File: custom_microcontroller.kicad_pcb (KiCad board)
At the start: 2 copper layers, 27.9 x 50.8 mm, 29 parts, among them J1 Conn_01x05_Male, J2 Conn_01x02_Male, J3 Conn_01x08_Male, J4 Conn_01x02_Male, J5 Conn_01x02_Male, J6 Conn_01x06_Male, J7 Conn_01x02_Male, U1 NCP1117ST33T3G, U2 STM32F042G6Ux, U3 SN65HVD233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

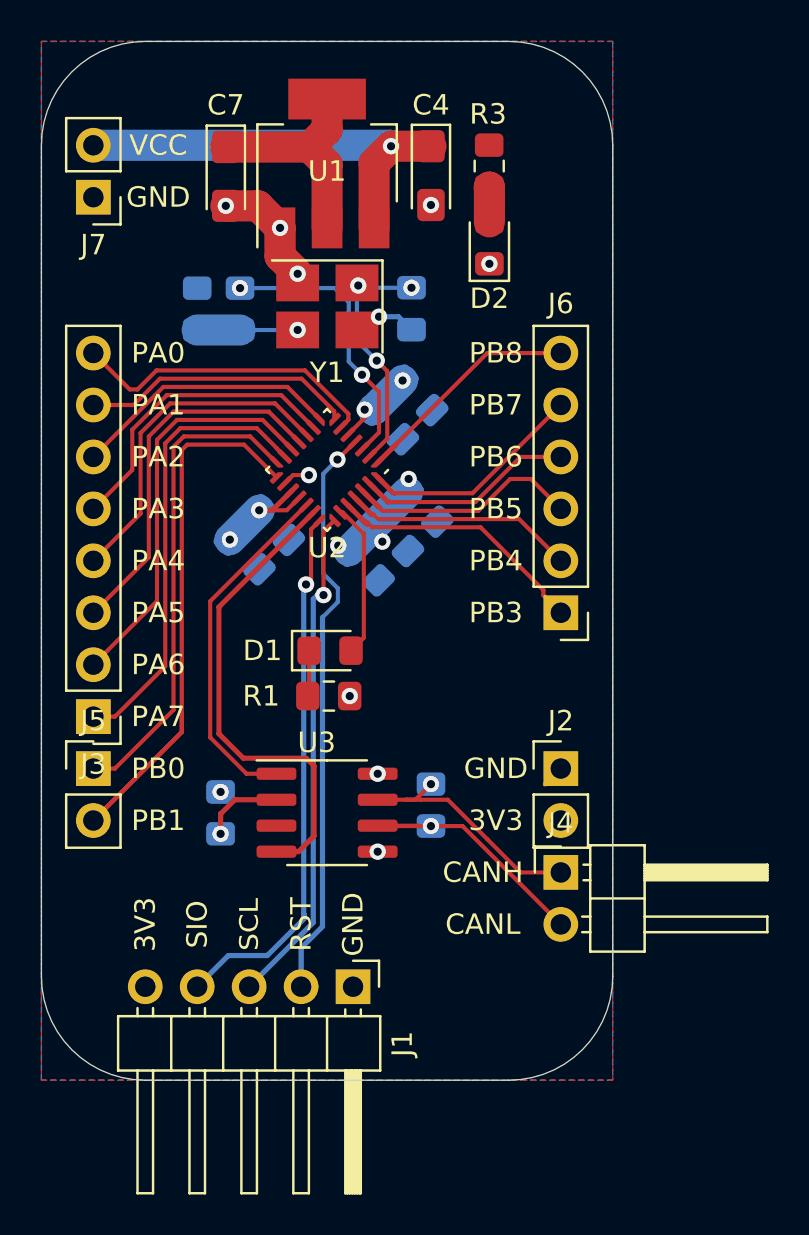
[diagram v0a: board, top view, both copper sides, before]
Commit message: panelized board
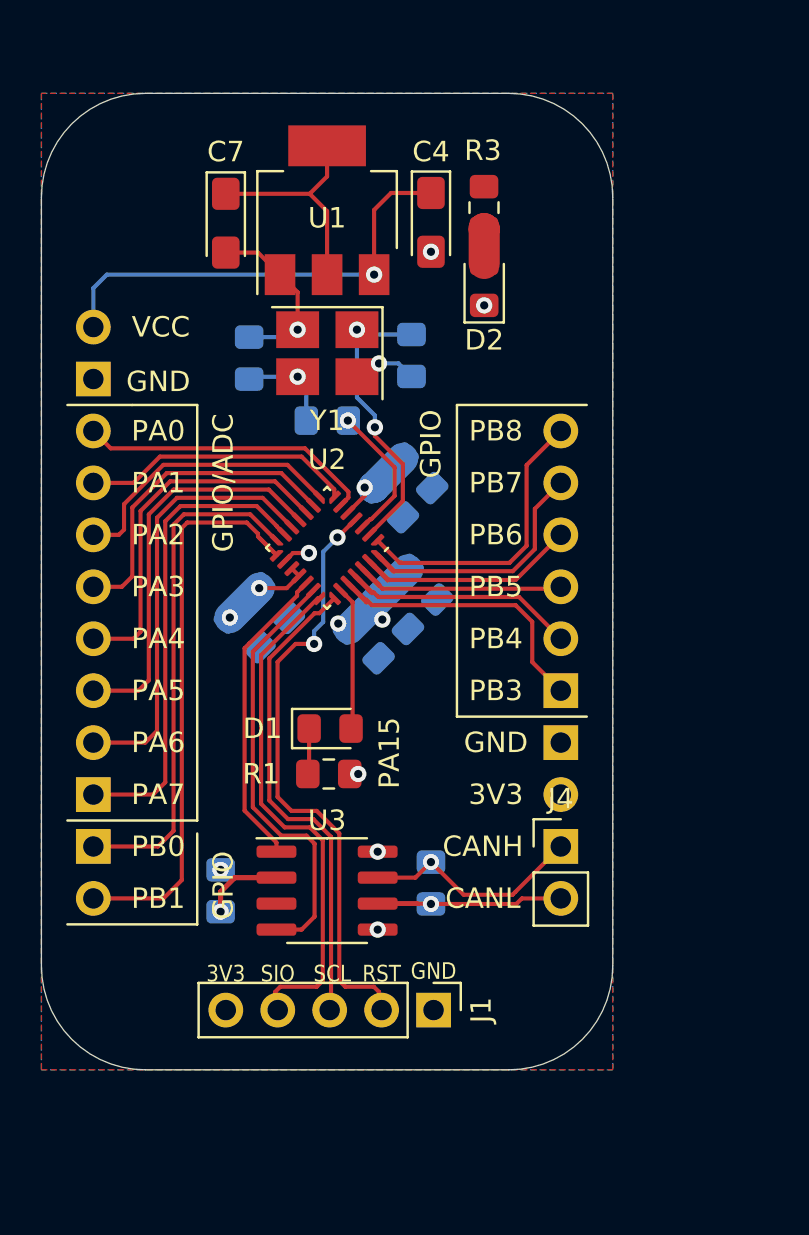
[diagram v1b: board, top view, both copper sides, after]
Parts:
- J1: footprint Connector_PinHeader_2.54mm:PinHeader_1x05_P2.54mm_Horizontal -> Connector_PinHeader_2.54mm:PinHeader_1x05_P2.54mm_Vertical
- J2, J3, J5, J6, J7: moved to B.Cu
- J4: footprint Connector_PinHeader_2.54mm:PinHeader_1x02_P2.54mm_Horizontal -> Connector_PinHeader_2.54mm:PinHeader_1x02_P2.54mm_Vertical
- moved J7 8.89 mm to (127.0, 120.7), turned to 0 degrees
- moved R2 6.92 mm to (138.4, 122.7), turned to 180 degrees
- moved J1 4.10 mm to (143.6, 151.5)
- moved C1 3.81 mm to (134.4, 133.0)
- moved C11 3.81 mm to (141.7, 132.1)
- moved C12 3.81 mm to (133.2, 145.7)
- moved C8 3.81 mm to (141.4, 126.7)
- moved C9 3.81 mm to (140.2, 133.6)
- moved J3 3.81 mm to (127.0, 141.0), turned to 0 degrees
- moved J5 3.81 mm to (127.0, 143.5), turned to 180 degrees
- moved R4 3.81 mm to (143.5, 145.3)
- moved U2 3.81 mm to (138.4, 128.9)
- moved U3 3.81 mm to (138.4, 145.7)
- moved C10 3.81 mm to (143.1, 130.7)
- moved C5 3.81 mm to (135.8, 131.6)
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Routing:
- net /OSC_N: track 13.7 -> 6.86 mm, vias 2 -> 1
- net /PB1: track 32.3 -> 28.6 mm
- net +3V3: track 28.1 -> 25.6 mm, vias 8 -> 6
- net /OSC_P: track 12.0 -> 14.4 mm, vias 3 -> 2
- net /CAN_RX: track 23.6 -> 21.3 mm
- net /CAN_TX: track 17.3 -> 15.0 mm
- net /PB8: track 12.4 -> 14.4 mm
- net /CAN_N: track 12.9 -> 11.1 mm
- net /PA2: track 13.2 -> 14.6 mm
- net /PA6: track 19.9 -> 21.4 mm
- net GND: track 16.1 -> 17.6 mm, vias 11 -> 9
- net VCC: track 20.9 -> 22.2 mm
- net /NRST: track 28.5 -> 29.8 mm, vias 1 -> 2
- net /PA5: track 18.2 -> 19.5 mm
- net /PB0: track 23.8 -> 25.0 mm
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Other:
- board size 27.9 x 50.8 mm -> 27.9 x 47.8 mm
- board text added: "GPIO"
- board text added: "GPIO/ADC"
- board text added: "PA15"

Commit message: single layer design
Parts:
- added G***: LOGO, memes:little_creatures, B.Cu at (138.6, 116.6)
- C1, C10, C11, C12, C2, C3, C5, C6, C8, C9, R2, R4: moved to F.Cu
- moved C6 6.67 mm to (136.2, 125.6), turned to 180 degrees
- moved C1 5.54 mm to (136.0, 138.4), turned to 180 degrees
- moved C8 5.30 mm to (136.2, 127.6), turned to 180 degrees
- moved C12 5.20 mm to (136.0, 141.3), turned to 180 degrees
- moved R1 4.94 mm to (143.4, 139.0), turned to 270 degrees
- moved C5 4.72 mm to (136.0, 136.3), turned to 180 degrees
- moved U2 3.93 mm to (137.4, 132.7), turned to 270 degrees
- moved D1 2.84 mm to (141.1, 139.0), turned to 90 degrees
- moved C9 2.63 mm to (142.6, 134.8), turned to 0 degrees
- moved C11 1.08 mm to (142.6, 132.7), turned to 0 degrees
- moved R4 0.67 mm to (143.2, 145.9)
- moved C10 0.52 mm to (142.6, 130.7), turned to 0 degrees
- moved C2 0.34 mm to (142.2, 119.4)
- moved C3 0.25 mm to (134.6, 119.4)
- moved R2 0.21 mm to (138.5, 122.9)
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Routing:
- net GND: track 17.6 -> 1.26 mm, vias 9 -> 21
- net /PB1: track 28.6 -> 18.7 mm
- net /PA5: track 19.5 -> 9.75 mm
- net /PA6: track 21.4 -> 12.3 mm
- net /PA4: track 17.7 -> 8.91 mm
- net /PA7: track 23.3 -> 14.6 mm
- net /SWDIO: track 25.6 -> 18.1 mm
- net /PA3: track 15.7 -> 8.79 mm
- net /PB5: track 10.2 -> 16.8 mm
- net /CAN_RX: track 21.3 -> 15.2 mm
- net /SWCLK: track 23.8 -> 17.9 mm
- net /NRST: track 29.8 -> 25.5 mm
- net /PA2: track 14.6 -> 10.3 mm
- net /PB6: track 10.7 -> 14.7 mm
- net /CAN_TX: track 15.0 -> 11.0 mm
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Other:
- board text added: "An STM32F042 Microcontroller with a built in CAN transceiver and CANH + CANL outputs."
- board text added: "SmolBoi.exe V2.0.0"
- board text added: "chenry was here"
- board text removed: "PA15"
